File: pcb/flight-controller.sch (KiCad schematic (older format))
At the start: 23 parts, among them IC1 ATMEGA32-A, K1 CONN_3, K10 CONN_3, K2 CONN_3, K3 CONN_3, K4 CONN_3, K5 CONN_3, K6 CONN_3, K7 CONN_3, K8 CONN_3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

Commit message: lots of improvements to flight control and PCB
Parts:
- added C10: 10uF, symbol C
- added C11: 0.1uF, symbol C
- added C12, C5, C7, C8: 100nF, symbol C
- added C13: 0.01uF, symbol C
- added C9: 1uF, symbol C
- added R4: 10k, symbol R
- C1, C2: value C -> 22pF
- C3: value C -> 2200pF
- C4: value C -> 10nF
- C6: value C -> 0.1uF
- R1, R2, R3: value R -> 4.7k
- X1: value CRYSTAL -> 16MHz
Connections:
- net +3.3V: now also C10.1, C11.2, C12.1, C13.1
- net +5V: now also C8.2, C9.1, R4.2
- net GND: now also C10.2, C11.1, C12.2, C13.2, C5.1, C7.2, C8.1, C9.2
- net RESET: now also C7.1, R4.1
- net at IC1.29 (AREF): now also C5.2

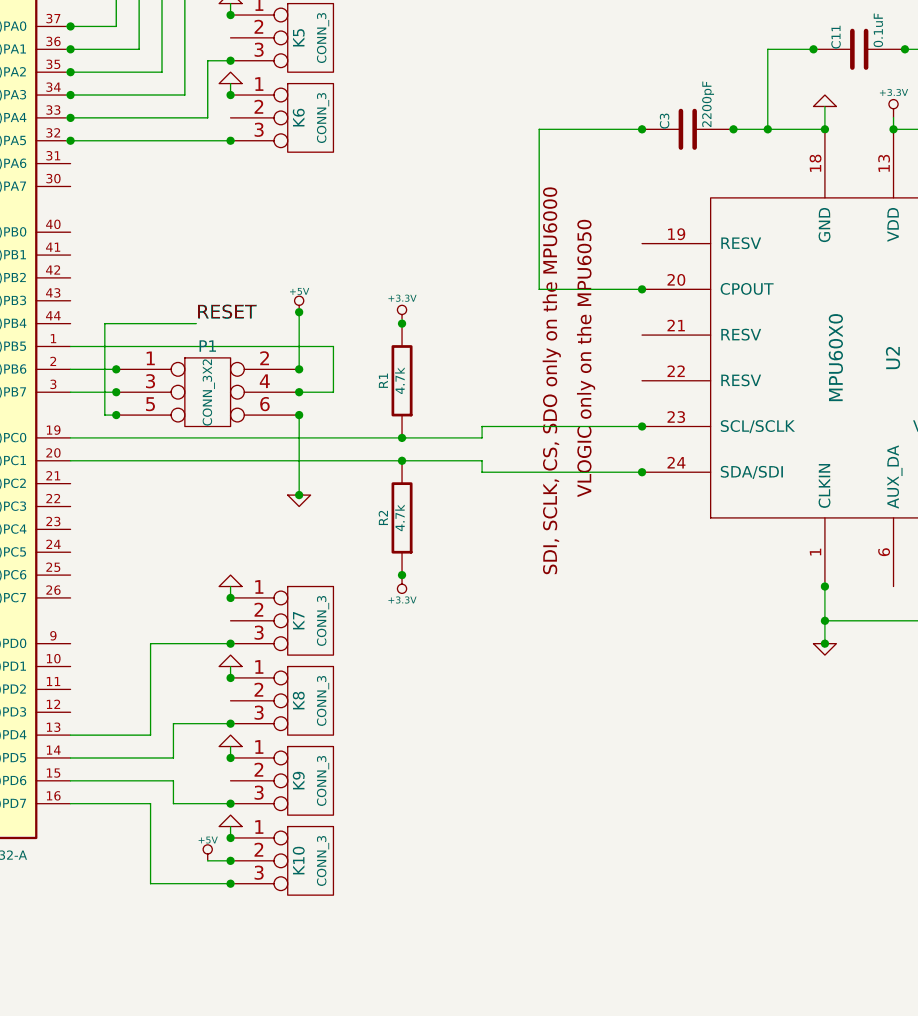
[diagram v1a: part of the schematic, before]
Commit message: finish yaw control, tune altitude correction
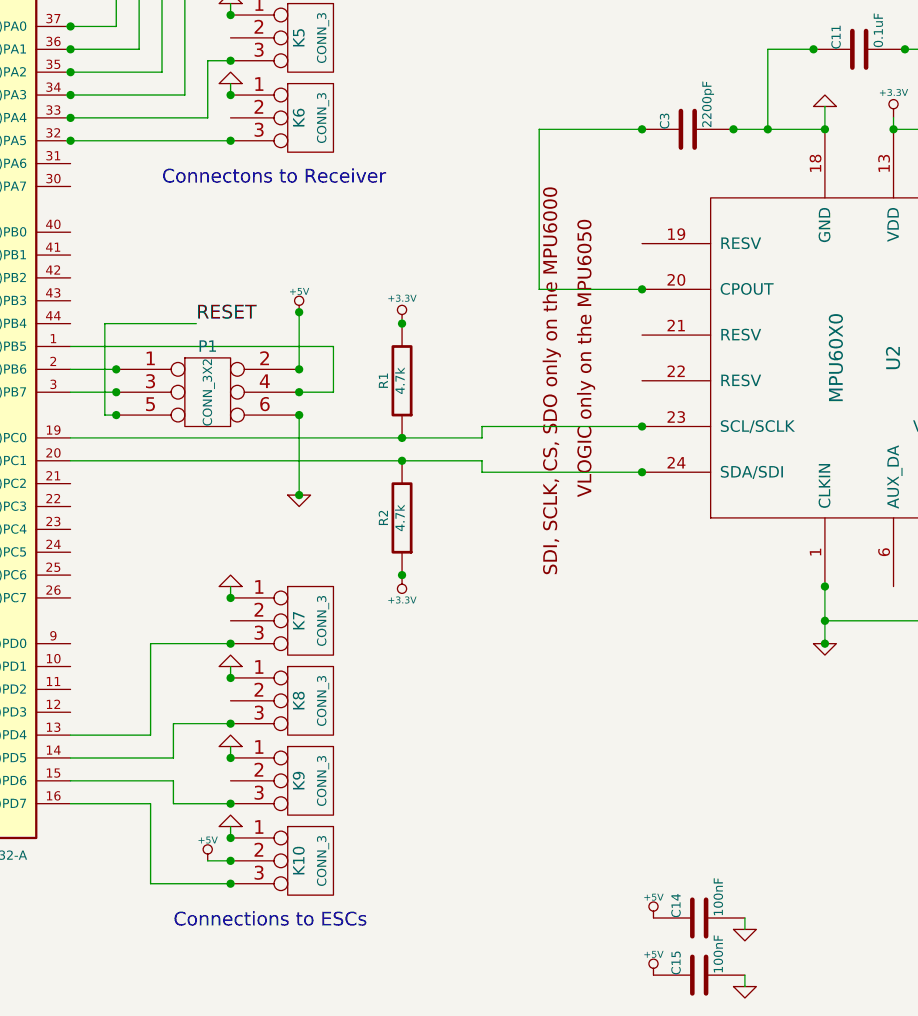
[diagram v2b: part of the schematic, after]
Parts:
- added C14, C15: 100nF, symbol C
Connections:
- net +5V: now also C14.1, C15.1
- net GND: now also C14.2, C15.2
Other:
- note added: "Connections to ESCs"
- note added: "Connectons to Receiver"
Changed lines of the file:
@@
 Connection ~ 4250 6100
 Connection ~ 2300 3850
+$Comp
+L C C14
+U 1 1 52BDAADF
+P 8050 6000
+F 0 "C14" H 8050 6100 40  0000 L CNN
+F 1 "100nF" H 8056 5915 40  0000 L CNN
+F 2 "" H 8088 5850 30  0000 C CNN
+F 3 "" H 8050 6000 60  0000 C CNN
+	1    8050 6000
+	0    -1   -1   0
+$EndComp
+$Comp
+L C C15
+U 1 1 52BDAAEE
+P 8050 6250
+F 0 "C15" H 8050 6350 40  0000 L CNN
+F 1 "100nF" H 8056 6165 40  0000 L CNN
+F 2 "" H 8088 6100 30  0000 C CNN
+F 3 "" H 8050 6250 60  0000 C CNN
+	1    8050 6250
+	0    -1   -1   0
+$EndComp
+$Comp
+L +5V #PWR028
+U 1 1 52BDAAFD
+P 7850 6000
+F 0 "#PWR028" H 7850 6090 20  0001 C CNN
+F 1 "+5V" H 7850 6090 30  0000 C CNN
+F 2 "" H 7850 6000 60  0000 C CNN
+F 3 "" H 7850 6000 60  0000 C CNN
+	1    7850 6000
+	1    0    0    -1
+$EndComp
+$Comp
+L +5V #PWR029
+U 1 1 52BDAB0C
+P 7850 6250
+F 0 "#PWR029" H 7850 6340 20  0001 C CNN
+F 1 "+5V" H 7850 6340 30  0000 C CNN
+F 2 "" H 7850 6250 60  0000 C CNN
+F 3 "" H 7850 6250 60  0000 C CNN
+	1    7850 6250
+	1    0    0    -1
+$EndComp
+$Comp
+L GND #PWR030
+U 1 1 52BDAB1B
+P 8250 6050
+F 0 "#PWR030" H 8250 6050 30  0001 C CNN
+F 1 "GND" H 8250 5980 30  0001 C CNN
+F 2 "" H 8250 6050 60  0000 C CNN
+F 3 "" H 8250 6050 60  0000 C CNN
+	1    8250 6050
+	1    0    0    -1
+$EndComp
+$Comp
+L GND #PWR031
+U 1 1 52BDAB2A
+P 8250 6300
+F 0 "#PWR031" H 8250 6300 30  0001 C CNN
+F 1 "GND" H 8250 6230 30  0001 C CNN
+F 2 "" H 8250 6300 60  0000 C CNN
+F 3 "" H 8250 6300 60  0000 C CNN
+	1    8250 6300
+	1    0    0    -1
+$EndComp
+Wire Wire Line
+	8250 6000 8250 6050
+Wire Wire Line
+	8250 6250 8250 6300
+Text Notes 5750 6050 0    60   ~ 0
+Connections to ESCs
+Text Notes 5700 2800 0    60   ~ 0
+Connectons to Receiver
 $EndSCHEMATC
